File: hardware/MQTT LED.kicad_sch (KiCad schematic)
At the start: 20 parts, among them J1 1x2P, J2 1x8P, J3 USB-TYPE-C-009, U1 ESPC2-M1-N2, U2 AL8860QMP-13, U3 AMS1117-3.3

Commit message: added todos
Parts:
- added R4: 5.1K, symbol Device:R
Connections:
- net CTRL: now also R4.1
- net GND: now also R4.2

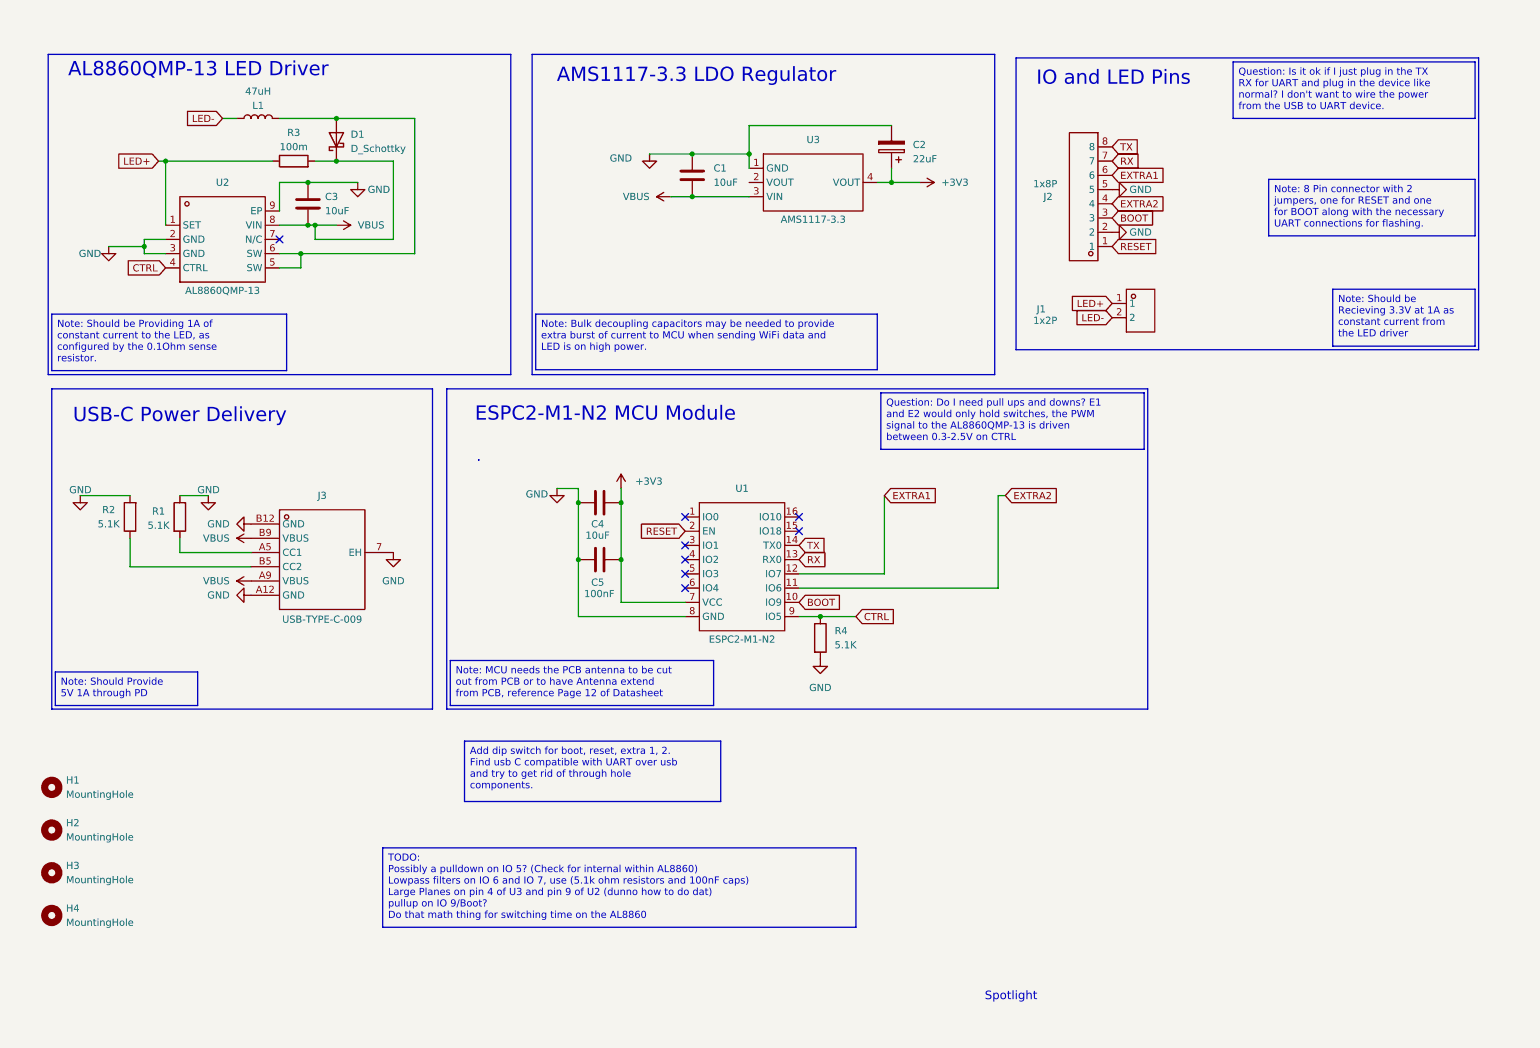
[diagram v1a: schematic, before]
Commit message: Switched to USB programming and ESP32-C3 module
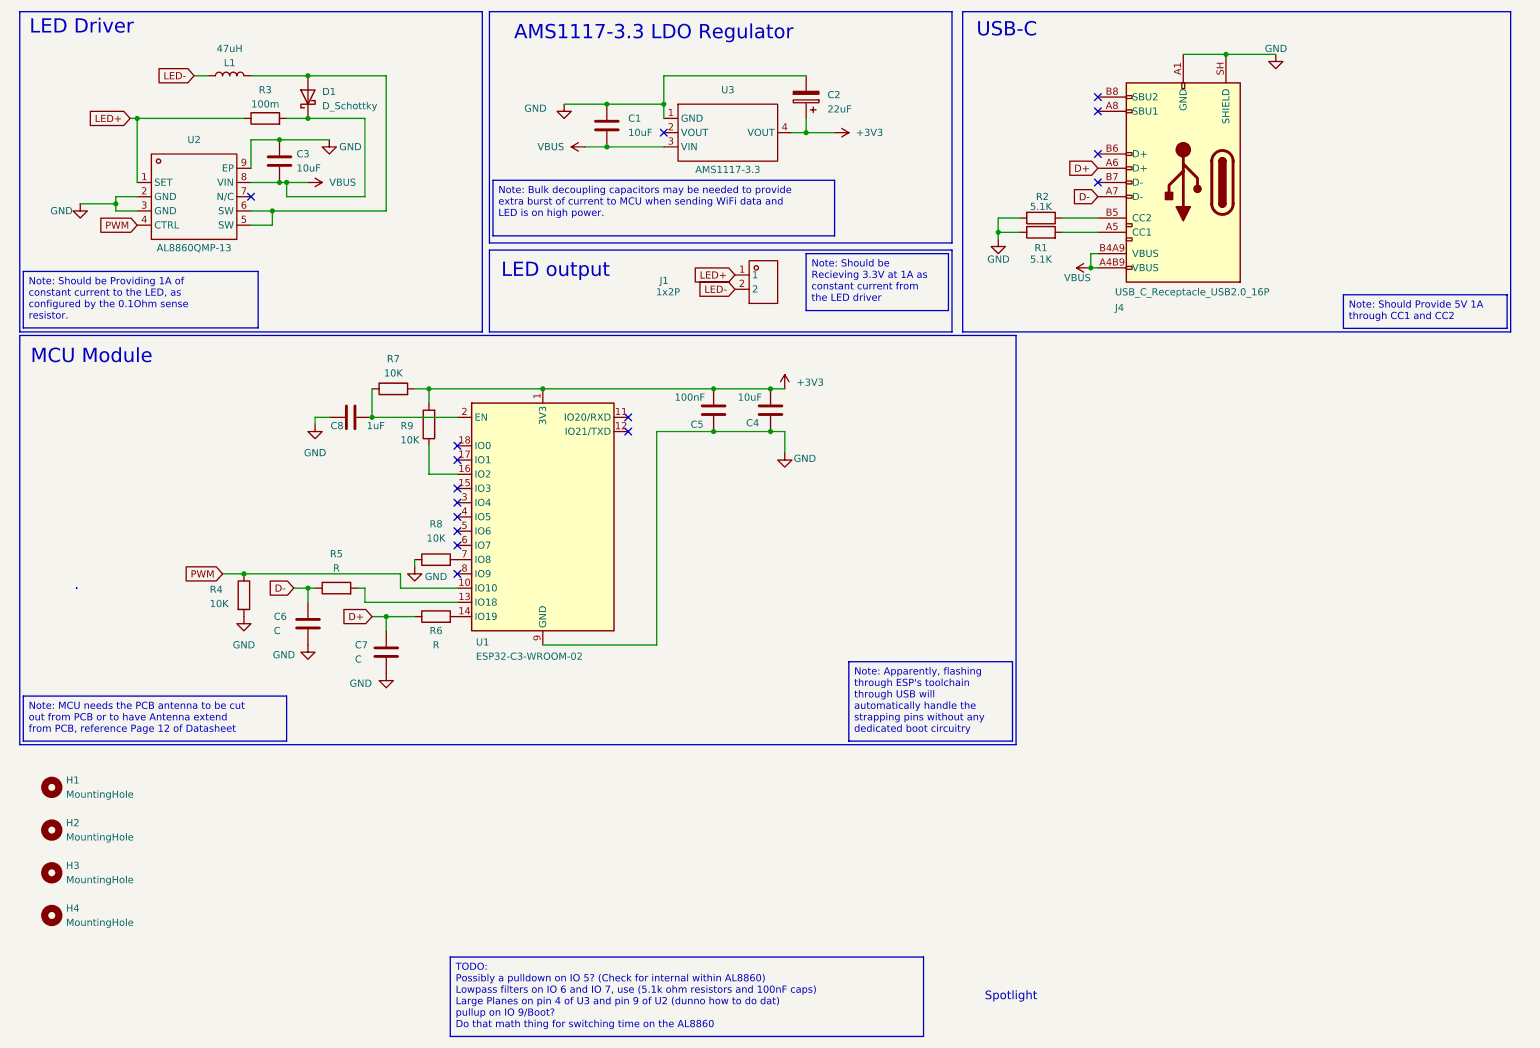
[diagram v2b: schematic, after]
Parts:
- removed J2: 1x8P, EasyEDA_Lib:HDR-TH_8P-P2.54-V-M-4, symbol EasyEDA_Lib:2541WV-08P
- removed J3: USB-TYPE-C-009, EasyEDA_Lib:TYPE-C-SMD_TYPE-C-6P, symbol EasyEDA_Lib:USB-TYPE-C-009
- removed U1: ESPC2-M1-N2, EasyEDA_Lib:WIFIM-SMD_ESPC2-M1, symbol EasyEDA_Lib:ESPC2-M1
- added C6, C7: C, EasyEDA_Lib:C0805, symbol Device:C
- added C8: 1uF, EasyEDA_Lib:C0805, symbol Device:C
- added J4: USB_C_Receptacle_USB2.0_16P, EasyEDA_Lib:TYPE-C-SMD_TYPE-C-3.1-16PIN, symbol Connector:USB_C_Receptacle_USB2.0_16P
- added R5, R6: R, EasyEDA_Lib:R0603, symbol Device:R
- added R7, R8, R9: 10K, EasyEDA_Lib:R0603, symbol Device:R
- added U1: ESP32-C3-WROOM-02, RF_Module:ESP32-C3-WROOM-02, symbol RF_Module:ESP32-C3-WROOM-02
- R4: value 5.1K -> 10K; footprint (none) -> EasyEDA_Lib:R0603
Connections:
- net +3V3: now also R7.2, R9.2, U1.1 (3V3)
- net GND: now also C6.2, C7.2, C8.1, J4.A1 (GND), J4.A12 (GND), J4.B1 (GND), J4.B12 (GND), J4.SH (SHIELD), R8.1, U1.19 (GND), U1.9 (GND)
- net VBUS: now also J4.A4B9 (VBUS), J4.A9 (VBUS), J4.B4 (VBUS), J4.B4A9 (VBUS), J4.B9 (VBUS)
- net at R2.1: now also J4.B5 (CC2)
- net at R1.2: now also J4.A5 (CC1)
- net CTRL renamed PWM
- net PWM: now also U1.10 (IO10)
- new net: R5.2, U1.13 (IO18)
- new net: R6.2, U1.14 (IO19)
- new net: R9.1, U1.16 (IO2)
- new net: C8.2, R7.1, U1.2 (EN)
- new net: R8.2, U1.7 (IO8)
- new net D+: C7.1, J4.A6 (D+), R6.1
- new net D-: C6.1, J4.A7 (D-), R5.1
- no-connect marks 8 -> 16
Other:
- note added: "LED Driver"
- note added: "LED output"
- note added: "MCU Module"
- note added: "USB-C"
- note removed: "AL8860QMP-13 LED Driver"
- note removed: "ESPC2-M1-N2 MCU Module"
- note removed: "IO and LED Pins"
- note removed: "USB-C Power Delivery"
- moved on the sheet: C1, C2, C3, C4, C5, D1, J1, L1, R1, R2, R3, R4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
